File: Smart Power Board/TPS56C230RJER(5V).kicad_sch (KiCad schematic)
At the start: 19 parts, among them IC1 TPS56C230RJER

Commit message: Feat[SmartPowerBoard]: MCU Development
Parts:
- renumbered IC1 to U4
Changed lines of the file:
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@@
 		(on_board yes)
 		(dnp no)
-		(property "Reference" "IC1"
+		(property "Reference" "U4"
 			(at 153.162 106.934 0)
 			(effects
@@
 			(project "SmartPowerBoard"
 				(path "/787a0061-c9d5-4e8d-b49f-b4e75e937f85/5dd8f6b1-552a-45c9-8a73-b8a0c181c148"
-					(reference "IC1")
+					(reference "U4")
 					(unit 1)
 				)

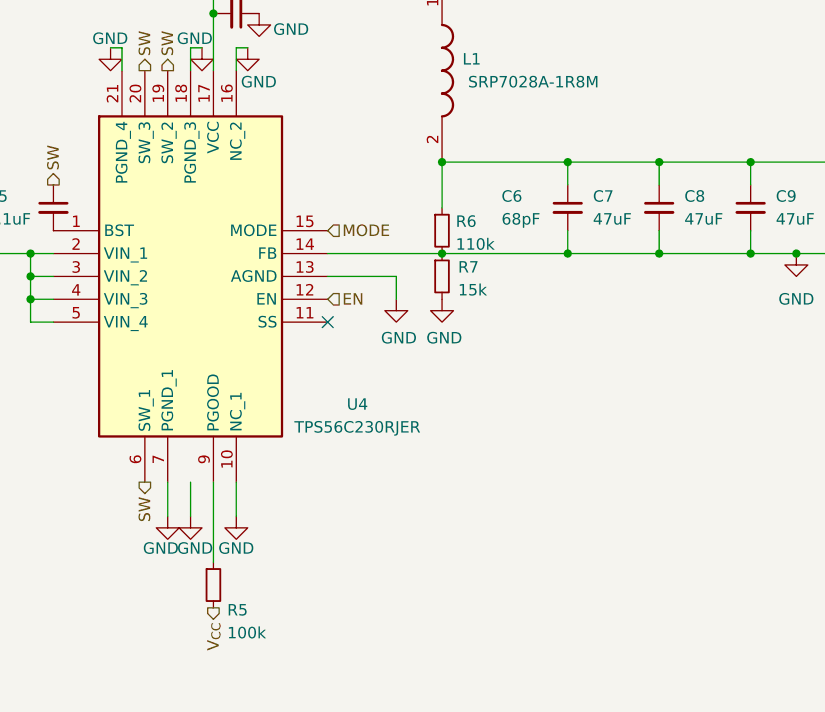
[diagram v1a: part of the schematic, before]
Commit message: Feat[SmartPowerBoard]:Starting Board Layout
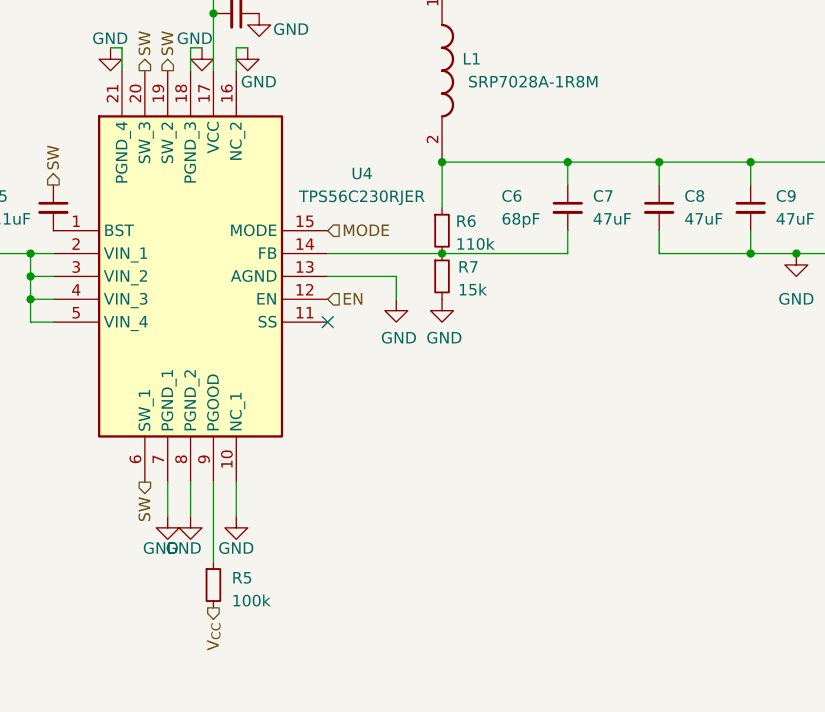
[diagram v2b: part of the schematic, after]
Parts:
- C1, C10, C2, C3, C4, C5, C7, C8, C9: footprint (none) -> Capacitor_SMD:C_0402_1005Metric
- C6: footprint (none) -> Capacitor_SMD:C_0201_0603Metric
- R1, R2, R3, R4, R5, R6, R7: footprint (none) -> Resistor_SMD:R_0402_1005Metric
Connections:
- net GND: now also U4.8 (PGND_2); no longer C6.2, R6.2, R7.1, U4.14 (FB)
- new net: C6.2, R6.2, R7.1, U4.14 (FB)

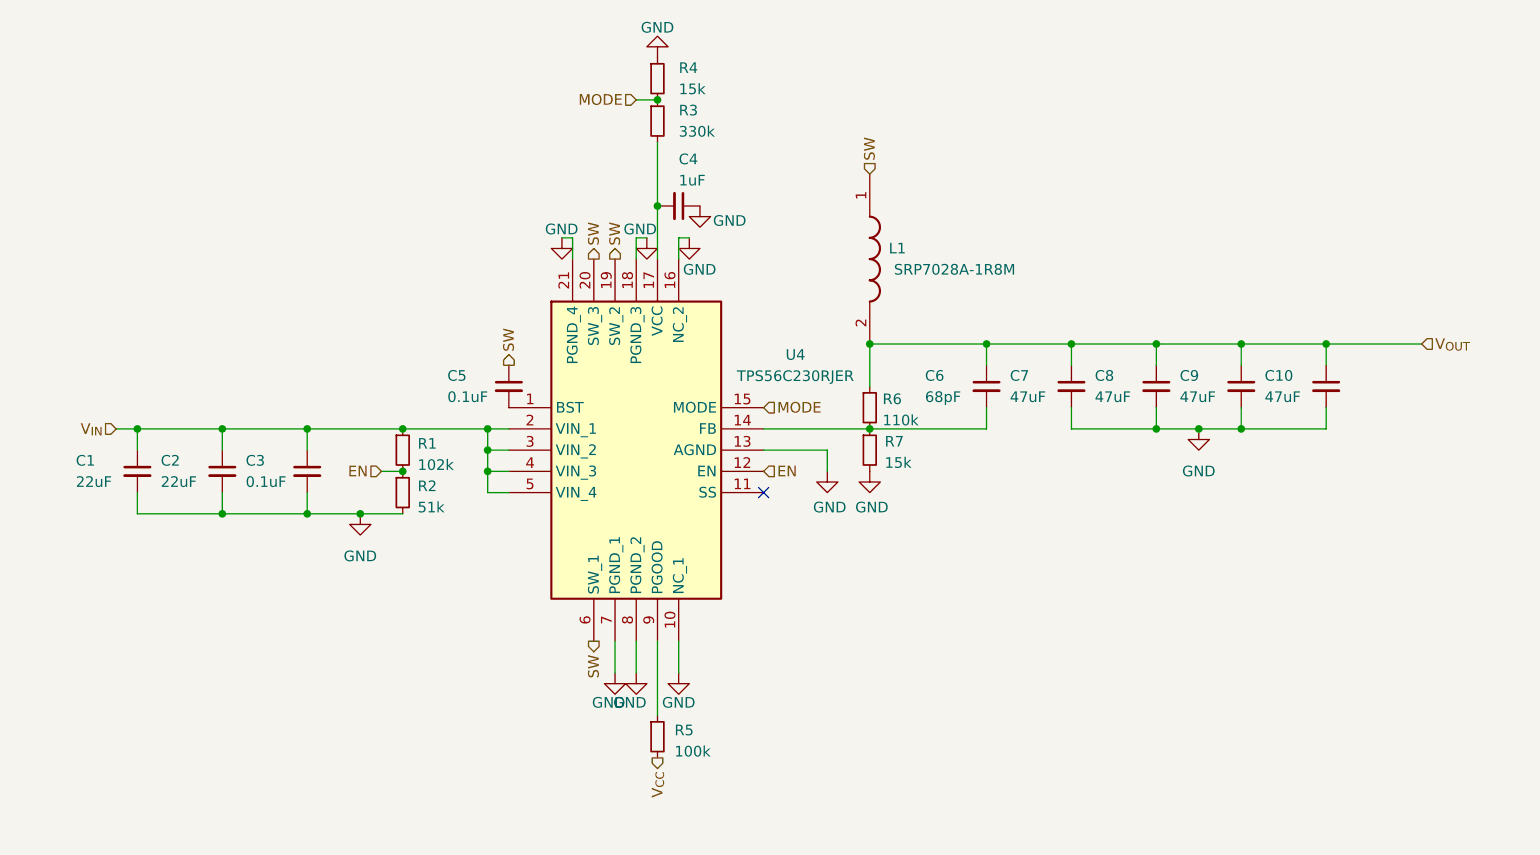
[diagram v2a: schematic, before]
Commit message: Feat[SmartPowerBoard]: Organized Schematic and New Buck
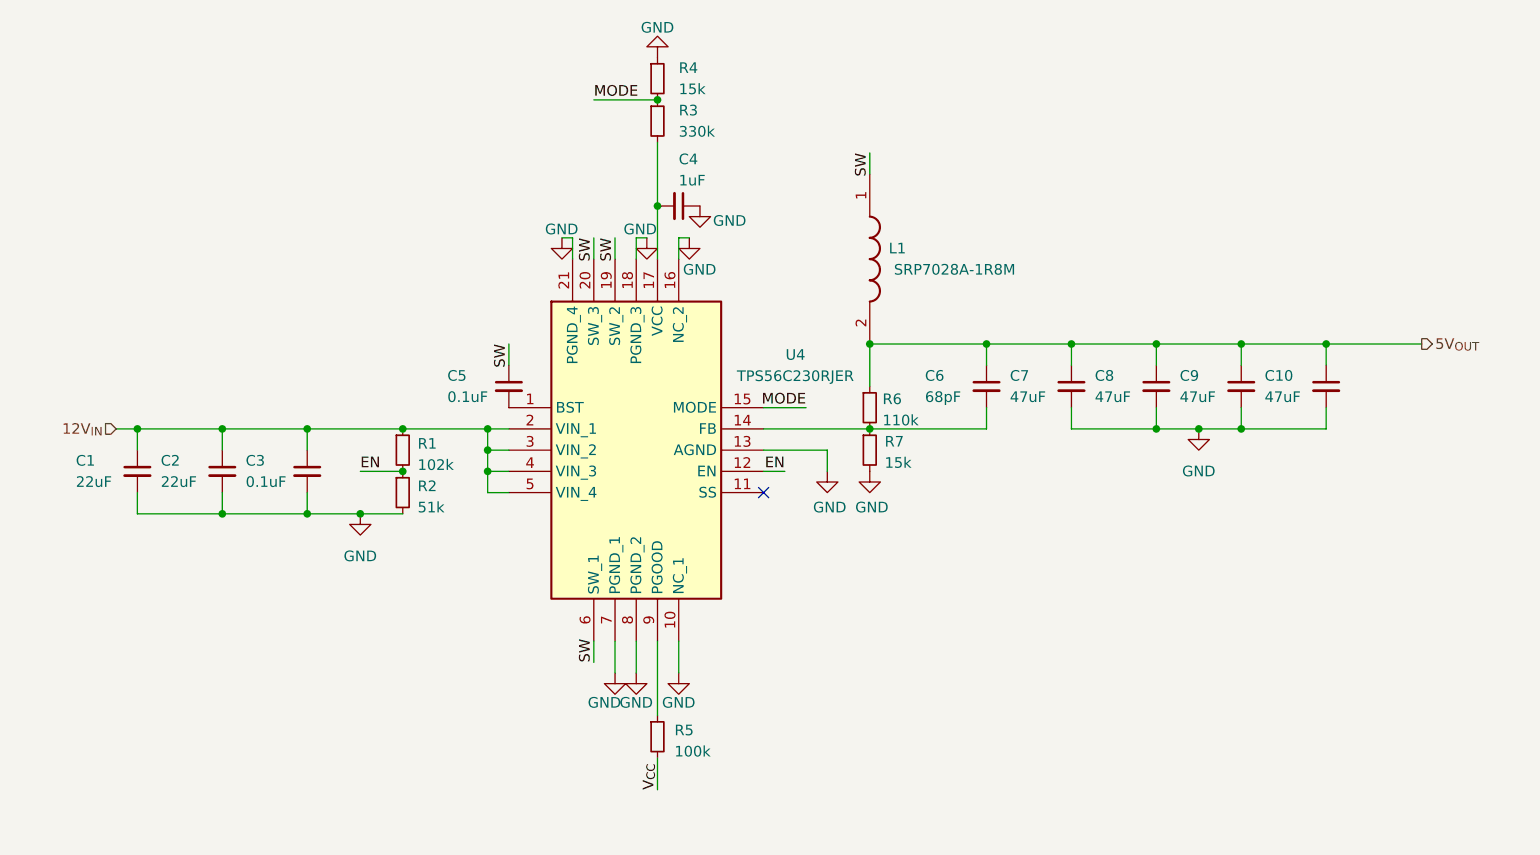
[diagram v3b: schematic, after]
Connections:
- net V_{IN} renamed 12V_{IN}
- net V_{OUT} renamed 5V_{OUT}
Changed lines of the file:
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@@
+	(wire
+		(pts
+			(xy 149.86 95.25) (xy 152.4 95.25)
+		)
+		(stroke
+			(width 0)
+			(type default)
+		)
+	)
 	(wire
 		(pts
@@
 	(wire
 		(pts
-			(xy 134.62 50.8) (xy 137.16 50.8)
+			(xy 129.54 50.8) (xy 137.16 50.8)
 		)
 		(stroke
@@
 	(wire
 		(pts
+			(xy 132.08 67.31) (xy 132.08 69.85)
+		)
+		(stroke
+			(width 0)
+			(type default)
+		)
+	)
+	(wire
+		(pts
 			(xy 176.53 80.01) (xy 186.69 80.01)
 		)
@@
 	(wire
 		(pts
+			(xy 119.38 80.01) (xy 119.38 82.55)
+		)
+		(stroke
+			(width 0)
+			(type default)
+		)
+	)
+	(wire
+		(pts
 			(xy 95.25 92.71) (xy 95.25 90.17)
 		)
@@
 	(wire
 		(pts
-			(xy 104.14 95.25) (xy 106.68 95.25)
+			(xy 101.6 95.25) (xy 106.68 95.25)
 		)
 		(stroke
@@
 	(wire
 		(pts
+			(xy 129.54 67.31) (xy 129.54 69.85)
+		)
+		(stroke
+			(width 0)
+			(type default)
+		)
+	)
+	(wire
+		(pts
 			(xy 186.69 80.01) (xy 196.85 80.01)
 		)
@@
 	(wire
 		(pts
+			(xy 129.54 118.11) (xy 129.54 115.57)
+		)
+		(stroke
+			(width 0)
+			(type default)
+		)
+	)
+	(wire
+		(pts
 			(xy 140.97 67.31) (xy 139.7 67.31)
 		)
@@
 	(wire
 		(pts
+			(xy 137.16 133.35) (xy 137.16 129.54)
+		)
+		(stroke
+			(width 0)
+			(type default)
+		)
+	)
+	(wire
+		(pts
 			(xy 207.01 90.17) (xy 217.17 90.17)
 		)
@@
 	(wire
 		(pts
+			(xy 154.94 87.63) (xy 149.86 87.63)
+		)
+		(stroke
+			(width 0)
+			(type default)
+		)
+	)
+	(wire
+		(pts
 			(xy 162.56 80.01) (xy 176.53 80.01)
 		)
@@
 	(wire
 		(pts
+			(xy 162.56 57.15) (xy 162.56 59.69)
+		)
+		(stroke
+			(width 0)
+			(type default)
+		)
+	)
+	(wire
+		(pts
 			(xy 139.7 119.38) (xy 139.7 115.57)
 		)
@@
 		)
 	)
-	(hierarchical_label "SW"
-		(shape input)
-		(at 162.56 59.69 90)
+	(label "SW"
+		(at 129.54 67.31 270)
 		(fields_autoplaced yes)
 		(effects
@@
 				(size 1.27 1.27)
 			)
-			(justify left)
-		)
-	)
-	(hierarchical_label "SW"
-		(shape output)
-		(at 129.54 115.57 270)
+			(justify right bottom)
+		)
+	)
+	(label "V_{CC}"
+		(at 137.16 133.35 90)
 		(fields_autoplaced yes)
 		(effects
@@
 				(size 1.27 1.27)
 			)
-			(justify right)
-		)
-	)
-	(hierarchical_label "V_{IN}"
+			(justify left bottom)
+		)
+	)
+	(label "SW"
+		(at 119.38 80.01 270)
+		(fields_autoplaced yes)
+		(effects
+			(font
+				(size 1.27 1.27)
+			)
+			(justify right bottom)
+		)
+	)
+	(label "SW"
+		(at 162.56 57.15 270)
+		(fields_autoplaced yes)
+		(effects
+			(font
+				(size 1.27 1.27)
+			)
+			(justify right bottom)
+		)
+	)
+	(label "MODE"
+		(at 154.94 87.63 180)
+		(fields_autoplaced yes)
+		(effects
+			(font
+				(size 1.27 1.27)
+			)
+			(justify right bottom)
+		)
+	)
+	(label "EN"
+		(at 101.6 95.25 0)
+		(fields_autoplaced yes)
+		(effects
+			(font
+				(size 1.27 1.27)
+			)
+			(justify left bottom)
+		)
+	)
+	(label "SW"
+		(at 132.08 67.31 270)
+		(fields_autoplaced yes)
+		(effects
+			(font
+				(size 1.27 1.27)
+			)
+			(justify right bottom)
+		)
+	)
+	(label "EN"
+		(at 152.4 95.25 180)
+		(fields_autoplaced yes)
+		(effects
+			(font
+				(size 1.27 1.27)
+			)
+			(justify right bottom)
+		)
+	)
+	(label "SW"
+		(at 129.54 118.11 90)
+		(fields_autoplaced yes)
+		(effects
+			(font
+				(size 1.27 1.27)
+			)
+			(justify left bottom)
+		)
+	)
+	(label "MODE"
+		(at 129.54 50.8 0)
+		(fields_autoplaced yes)
+		(effects
+			(font
+				(size 1.27 1.27)
+			)
+			(justify left bottom)
+		)
+	)
+	(hierarchical_label "12V_{IN}"
 		(shape input)
 		(at 72.39 90.17 180)
@@
 		)
 	)
-	(hierarchical_label "EN"
-		(shape input)
-		(at 149.86 95.25 0)
-		(fields_autoplaced yes)
-		(effects
-			(font
-				(size 1.27 1.27)
-			)
-			(justify left)
-		)
-	)
-	(hierarchical_label "MODE"
-		(shape input)
-		(at 134.62 50.8 180)
-		(fields_autoplaced yes)
-		(effects
-			(font
-				(size 1.27 1.27)
-			)
-			(justify right)
-		)
-	)
-	(hierarchical_label "V_{OUT}"
-		(shape input)
+	(hierarchical_label "5V_{OUT}"
+		(shape output)
 		(at 228.6 80.01 0)
 		(fields_autoplaced yes)
@@
 		)
 	)
-	(hierarchical_label "SW"
-		(shape output)
-		(at 119.38 82.55 90)
-		(fields_autoplaced yes)
-		(effects
-			(font
-				(size 1.27 1.27)
-			)
-			(justify left)
-		)
-	)
-	(hierarchical_label "EN"
-		(shape input)
-		(at 104.14 95.25 180)
-		(fields_autoplaced yes)
-		(effects
-			(font
-				(size 1.27 1.27)
-			)
-			(justify right)
-		)
-	)
-	(hierarchical_label "MODE"
-		(shape input)
-		(at 149.86 87.63 0)
-		(fields_autoplaced yes)
-		(effects
-			(font
-				(size 1.27 1.27)
-			)
-			(justify left)
-		)
-	)
-	(hierarchical_label "SW"
-		(shape output)
-		(at 129.54 69.85 90)
-		(fields_autoplaced yes)
-		(effects
-			(font
-				(size 1.27 1.27)
-			)
-			(justify left)
-		)
-	)
-	(hierarchical_label "SW"
-		(shape output)
-		(at 132.08 69.85 90)
-		(fields_autoplaced yes)
-		(effects
-			(font
-				(size 1.27 1.27)
-			)
-			(justify left)
-		)
-	)
-	(hierarchical_label "V_{CC}"
-		(shape output)
-		(at 137.16 129.54 270)
-		(fields_autoplaced yes)
-		(effects
-			(font
-				(size 1.27 1.27)
-			)
-			(justify right)
-		)
-	)
 	(symbol
 		(lib_id "Device:C_Small")
@@
 		)
 		(property "Value" "GND"
-			(at 133.858 122.936 0)
+			(at 134.62 122.936 0)
 			(effects
 				(font
@@
 		)
 		(property "Value" "GND"
-			(at 131.318 122.936 0)
-			(effects
-				(font
+			(at 130.81 122.936 0)
+			(effects
+				(font

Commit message: Feat[SmartPowerBoard]: Routing
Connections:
- net V_{CC}: now also C4.2, R3.2, U4.17 (VCC)
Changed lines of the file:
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@@
+	)
+	(junction
+		(at 137.16 57.15)
+		(diameter 0)
+		(color 0 0 0 0)
 	)
 	(junction
@@
 	(wire
 		(pts
-			(xy 137.16 55.88) (xy 137.16 63.5)
+			(xy 137.16 55.88) (xy 137.16 57.15)
 		)
 		(stroke
@@
 	(wire
 		(pts
+			(xy 129.54 57.15) (xy 137.16 57.15)
+		)
+		(stroke
+			(width 0)
+			(type default)
+		)
+	)
+	(wire
+		(pts
 			(xy 217.17 87.63) (xy 217.17 90.17)
 		)
@@
 		(pts
 			(xy 116.84 90.17) (xy 119.38 90.17)
+		)
+		(stroke
+			(width 0)
+			(type default)
+		)
+	)
+	(wire
+		(pts
+			(xy 137.16 57.15) (xy 137.16 63.5)
 		)
 		(stroke
@@
 		)
 	)
+	(label "V_{CC}"
+		(at 129.54 57.15 0)
+		(fields_autoplaced yes)
+		(effects
+			(font
+				(size 1.27 1.27)
+			)
+			(justify left bottom)
+		)
+	)
 	(label "EN"
 		(at 101.6 95.25 0)
@@
 	(label "SW"
 		(at 132.08 67.31 270)
-		(fields_autoplaced yes)
-		(effects
-			(font
-				(size 1.27 1.27)
-			)
-			(justify right bottom)
-		)
-	)
-	(label "EN"
-		(at 152.4 95.25 180)
 		(fields_autoplaced yes)
 		(effects
@@
 		)
 	)
+	(hierarchical_label "EN"
+		(shape input)
+		(at 152.4 95.25 0)
+		(fields_autoplaced yes)
+		(effects
+			(font
+				(size 1.27 1.27)
+			)
+			(justify left)
+		)
+	)

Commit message: Feat[SmartPowerBoard]: Silkscreen + Ground
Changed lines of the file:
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@@
 (kicad_sch
-	(version 20240101)
+	(version 20241004)
 	(generator "eeschema")
 	(generator_version "8.99")

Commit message: Feat[SmartPowerBoard]: Tapeout
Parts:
- C1, C10, C2, C7, C8, C9: footprint Capacitor_SMD:C_0402_1005Metric -> Capacitor_SMD:C_0603_1608Metric
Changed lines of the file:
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@@
 			)
 		)
-		(property "Footprint" "Capacitor_SMD:C_0402_1005Metric"
+		(property "Footprint" "Capacitor_SMD:C_0603_1608Metric"
 			(at 74.93 95.25 0)
 			(effects
@@
 			)
 		)
-		(property "Footprint" "Capacitor_SMD:C_0402_1005Metric"
+		(property "Footprint" "Capacitor_SMD:C_0603_1608Metric"
 			(at 186.69 85.09 0)
 			(effects
@@
 			)
 		)
-		(property "Footprint" "Capacitor_SMD:C_0402_1005Metric"
+		(property "Footprint" "Capacitor_SMD:C_0603_1608Metric"
 			(at 207.01 85.09 0)
 			(effects
@@
 			)
 		)
-		(property "Footprint" "Capacitor_SMD:C_0402_1005Metric"
+		(property "Footprint" "Capacitor_SMD:C_0603_1608Metric"
 			(at 217.17 85.09 0)
 			(effects
@@
 			)
 		)
-		(property "Footprint" "Capacitor_SMD:C_0402_1005Metric"
+		(property "Footprint" "Capacitor_SMD:C_0603_1608Metric"
 			(at 85.09 95.25 0)
 			(effects
@@
 			)
 		)
-		(property "Footprint" "Capacitor_SMD:C_0402_1005Metric"
+		(property "Footprint" "Capacitor_SMD:C_0603_1608Metric"
 			(at 196.85 85.09 0)
 			(effects
